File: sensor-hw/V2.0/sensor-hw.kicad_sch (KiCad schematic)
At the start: 0 parts

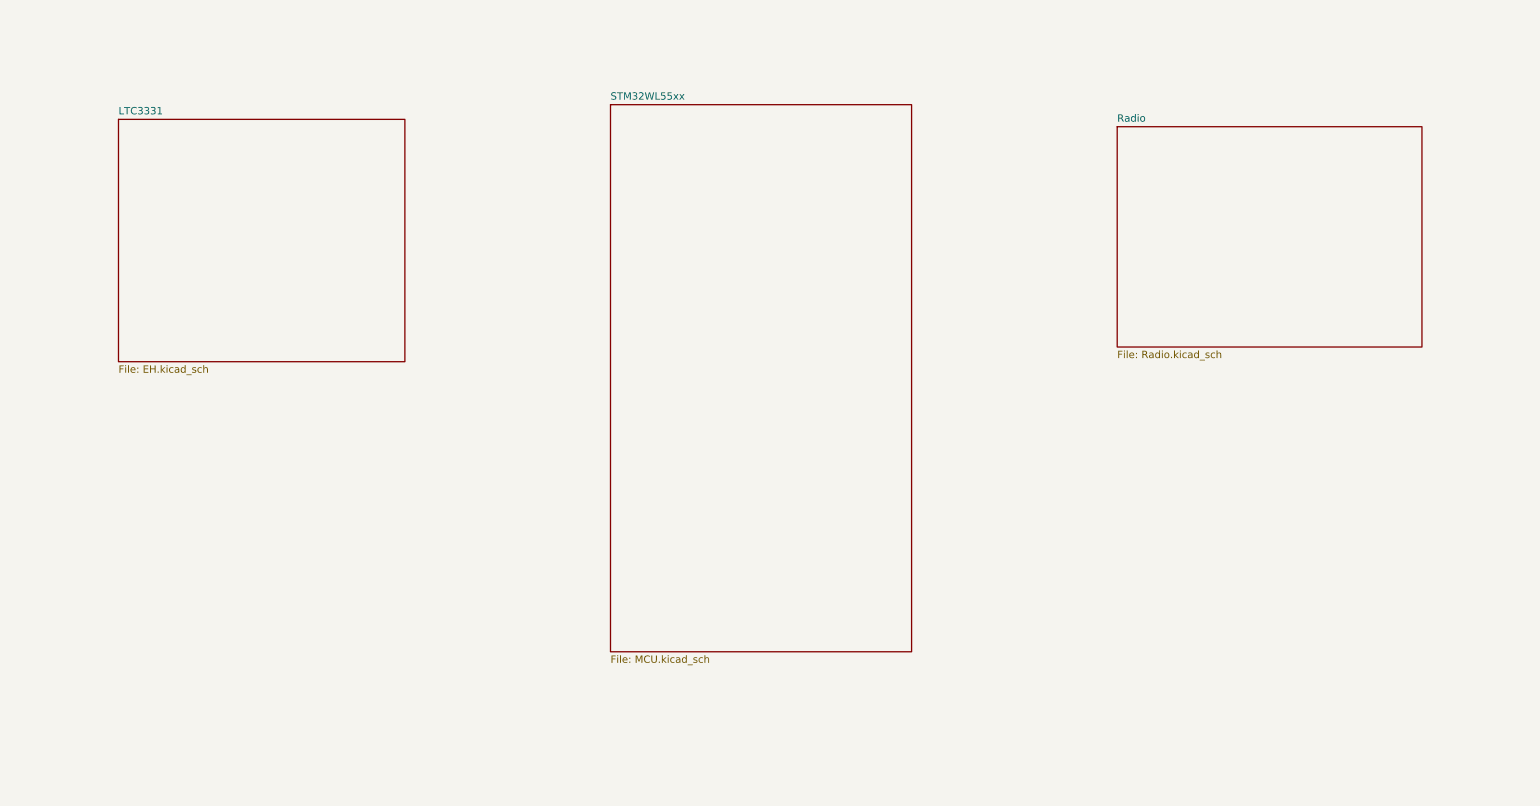
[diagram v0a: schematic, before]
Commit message: rearranged heirchal block wiring for better representation.
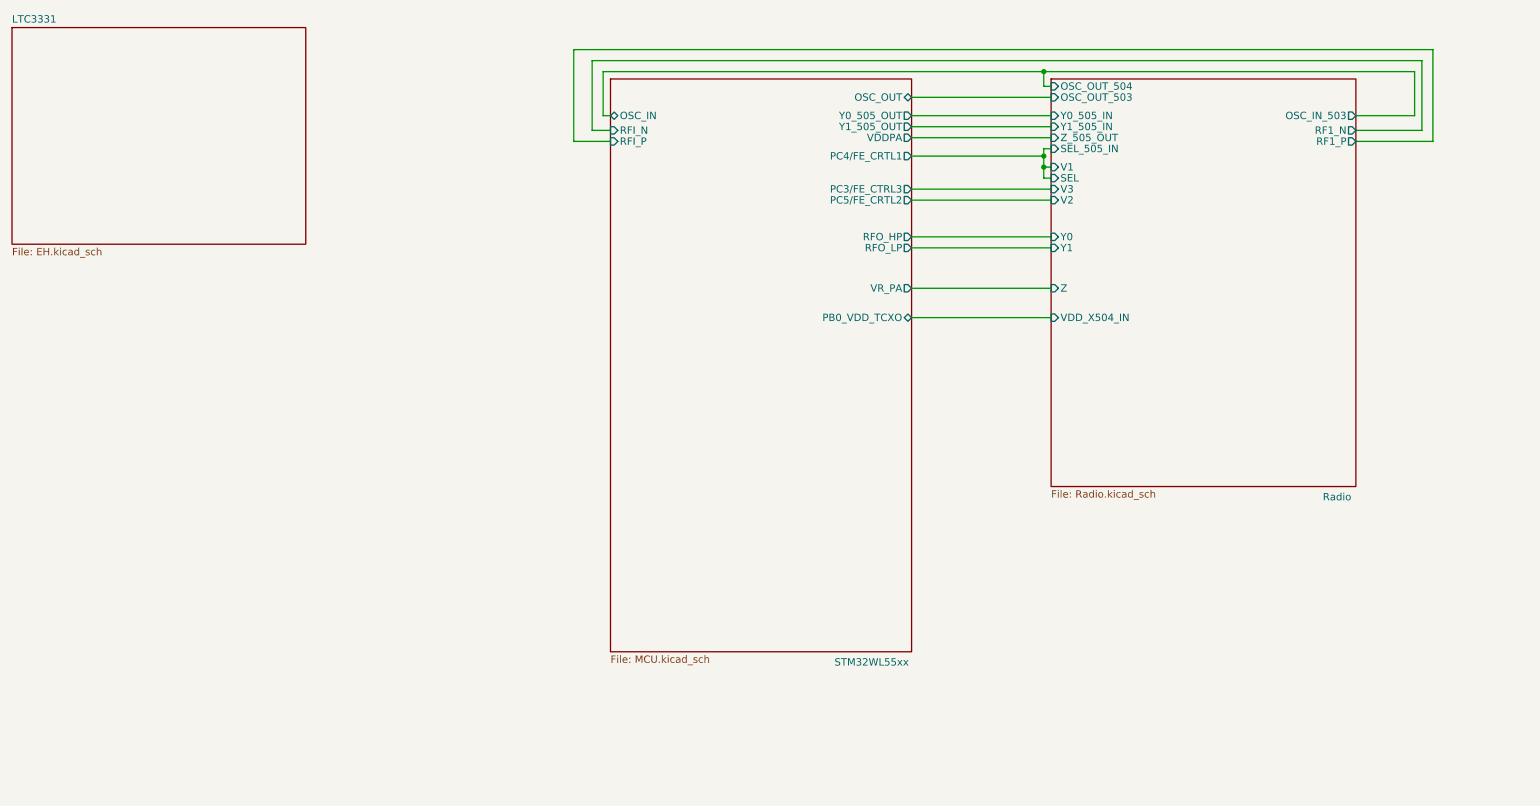
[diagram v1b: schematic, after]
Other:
- sheet Radio ports: added OSC_IN_503, OSC_OUT_503, OSC_OUT_504, RF1_N, RF1_P, SEL, SEL_505_IN, V1, V2, V3, VDD_X504_IN, Y0, Y0_505_IN, Y1, Y1_505_IN, Z, Z_505_OUT; removed none
- sheet STM32WL55xx ports: added OSC_IN, OSC_OUT, PB0_VDD_TCXO, PC3/FE_CTRL3, PC4/FE_CRTL1, PC5/FE_CRTL2, RFI_N, RFI_P, RFO_HP, RFO_LP, VDDPA, VR_PA, Y0_505_OUT, Y1_505_OUT; removed none
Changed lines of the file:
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@@
 (kicad_sch (version 20230121) (generator eeschema)
   (paper "A4")
-  (sheet (at 34.925 37.465) (size 49.53 41.91) (fields_autoplaced)
+  (junction (at 194.945 45.72) (diameter 0) (color 0 0 0 0)
+  )
+  (junction (at 194.945 29.21) (diameter 0) (color 0 0 0 0)
+  )
+  (junction (at 194.945 43.815) (diameter 0) (color 0 0 0 0)
+  )
+  (wire (pts (xy 260.35 39.37) (xy 260.35 27.305))
+    (stroke (width 0) (type default))
+  )
+  (wire (pts (xy 194.945 47.625) (xy 196.215 47.625))
+    (stroke (width 0) (type default))
+  )
+  (wire (pts (xy 172.085 33.655) (xy 196.215 33.655))
+    (stroke (width 0) (type default))
+  )
+  (wire (pts (xy 172.085 49.53) (xy 196.215 49.53))
+    (stroke (width 0) (type default))
+  )
+  (wire (pts (xy 172.085 57.785) (xy 196.215 57.785))
+    (stroke (width 0) (type default))
+  )
+  (wire (pts (xy 196.215 31.75) (xy 194.945 31.75))
+    (stroke (width 0) (type default))
+  )
+  (wire (pts (xy 194.945 45.72) (xy 196.215 45.72))
+    (stroke (width 0) (type default))
+  )
+  (wire (pts (xy 172.085 66.675) (xy 196.215 66.675))
+    (stroke (width 0) (type default))
+  )
+  (wire (pts (xy 172.085 36.83) (xy 196.215 36.83))
+    (stroke (width 0) (type default))
+  )
+  (wire (pts (xy 194.945 31.75) (xy 194.945 29.21))
+    (stroke (width 0) (type default))
+  )
+  (wire (pts (xy 172.085 38.735) (xy 196.215 38.735))
+    (stroke (width 0) (type default))
+  )
+  (wire (pts (xy 113.665 41.275) (xy 120.015 41.275))
+    (stroke (width 0) (type default))
+  )
+  (wire (pts (xy 194.945 43.815) (xy 194.945 45.72))
+    (stroke (width 0) (type default))
+  )
+  (wire (pts (xy 118.745 36.83) (xy 118.745 29.21))
+    (stroke (width 0) (type default))
+  )
+  (wire (pts (xy 172.085 51.435) (xy 196.215 51.435))
+    (stroke (width 0) (type default))
+  )
+  (wire (pts (xy 118.745 29.21) (xy 194.945 29.21))
+    (stroke (width 0) (type default))
+  )
+  (wire (pts (xy 262.255 41.275) (xy 262.255 25.4))
+    (stroke (width 0) (type default))
+  )
+  (wire (pts (xy 172.085 40.64) (xy 196.215 40.64))
+    (stroke (width 0) (type default))
+  )
+  (wire (pts (xy 172.085 59.69) (xy 196.215 59.69))
+    (stroke (width 0) (type default))
+  )
+  (wire (pts (xy 248.92 41.275) (xy 262.255 41.275))
+    (stroke (width 0) (type default))
+  )
+  (wire (pts (xy 172.085 43.815) (xy 194.945 43.815))
+    (stroke (width 0) (type default))
+  )
+  (wire (pts (xy 248.92 39.37) (xy 260.35 39.37))
+    (stroke (width 0) (type default))
+  )
+  (wire (pts (xy 116.84 27.305) (xy 116.84 39.37))
+    (stroke (width 0) (type default))
+  )
+  (wire (pts (xy 248.92 36.83) (xy 259.08 36.83))
+    (stroke (width 0) (type default))
+  )
+  (wire (pts (xy 194.945 29.21) (xy 259.08 29.21))
+    (stroke (width 0) (type default))
+  )
+  (wire (pts (xy 262.255 25.4) (xy 113.665 25.4))
+    (stroke (width 0) (type default))
+  )
+  (wire (pts (xy 172.085 71.755) (xy 196.215 71.755))
+    (stroke (width 0) (type default))
+  )
+  (wire (pts (xy 260.35 27.305) (xy 116.84 27.305))
+    (stroke (width 0) (type default))
+  )
+  (wire (pts (xy 113.665 25.4) (xy 113.665 41.275))
+    (stroke (width 0) (type default))
+  )
+  (wire (pts (xy 120.015 36.83) (xy 118.745 36.83))
+    (stroke (width 0) (type default))
+  )
+  (wire (pts (xy 194.945 43.815) (xy 194.945 42.545))
+    (stroke (width 0) (type default))
+  )
+  (wire (pts (xy 259.08 29.21) (xy 259.08 36.83))
+    (stroke (width 0) (type default))
+  )
+  (wire (pts (xy 194.945 45.72) (xy 194.945 47.625))
+    (stroke (width 0) (type default))
+  )
+  (wire (pts (xy 194.945 42.545) (xy 196.215 42.545))
+    (stroke (width 0) (type default))
+  )
+  (wire (pts (xy 116.84 39.37) (xy 120.015 39.37))
+    (stroke (width 0) (type default))
+  )
+  (sheet (at 16.51 21.59) (size 50.8 37.465) (fields_autoplaced)
     (stroke (width 0.1524) (type solid))
     (fill (color 0 0 0 0.0000))
-    (property "Sheetname" "LTC3331" (at 34.925 36.7534 0)
+    (property "Sheetname" "LTC3331" (at 16.51 20.8784 0)
       (effects (font (size 1.27 1.27)) (justify left bottom))
     )
-    (property "Sheetfile" "EH.kicad_sch" (at 34.925 79.9596 0)
+    (property "Sheetfile" "EH.kicad_sch" (at 16.51 59.6396 0)
       (effects (font (size 1.27 1.27)) (justify left top))
     )
@@
     )
   )
-  (sheet (at 120.015 34.925) (size 52.07 94.615) (fields_autoplaced)
+  (sheet (at 120.015 30.48) (size 52.07 99.06)
     (stroke (width 0.1524) (type solid))
     (fill (color 0 0 0 0.0000))
-    (property "Sheetname" "STM32WL55xx" (at 120.015 34.2134 0)
+    (property "Sheetname" "STM32WL55xx" (at 158.75 132.08 0)
       (effects (font (size 1.27 1.27)) (justify left bottom))
     )
     (property "Sheetfile" "MCU.kicad_sch" (at 120.015 130.1246 0)
       (effects (font (size 1.27 1.27)) (justify left top))
+    )
+    (pin "Y1_505_OUT" output (at 172.085 38.735 0)
+      (effects (font (size 1.27 1.27)) (justify right))
+    )
+    (pin "PC3{slash}FE_CTRL3" output (at 172.085 49.53 0)
+      (effects (font (size 1.27 1.27)) (justify right))
+    )
+    (pin "PC4{slash}FE_CRTL1" output (at 172.085 43.815 0)
+      (effects (font (size 1.27 1.27)) (justify right))
+    )
+    (pin "PC5{slash}FE_CRTL2" output (at 172.085 51.435 0)
+      (effects (font (size 1.27 1.27)) (justify right))
+    )
+    (pin "VDDPA" output (at 172.085 40.64 0)
+      (effects (font (size 1.27 1.27)) (justify right))
+    )
+    (pin "RFI_P" input (at 120.015 41.275 180)
+      (effects (font (size 1.27 1.27)) (justify left))
+    )
+    (pin "RFO_LP" output (at 172.085 59.69 0)
+      (effects (font (size 1.27 1.27)) (justify right))
+    )
+    (pin "OSC_OUT" bidirectional (at 172.085 33.655 0)
+      (effects (font (size 1.27 1.27)) (justify right))
+    )
+    (pin "OSC_IN" bidirectional (at 120.015 36.83 180)
+      (effects (font (size 1.27 1.27)) (justify left))
+    )
+    (pin "VR_PA" output (at 172.085 66.675 0)
+      (effects (font (size 1.27 1.27)) (justify right))
+    )
+    (pin "Y0_505_OUT" output (at 172.085 36.83 0)
+      (effects (font (size 1.27 1.27)) (justify right))
+    )
+    (pin "RFI_N" input (at 120.015 39.37 180)
+      (effects (font (size 1.27 1.27)) (justify left))
+    )
+    (pin "RFO_HP" output (at 172.085 57.785 0)
+      (effects (font (size 1.27 1.27)) (justify right))
+    )
+    (pin "PB0_VDD_TCXO" bidirectional (at 172.085 71.755 0)
+      (effects (font (size 1.27 1.27)) (justify right))
     )
     (instances
@@
     )
   )
-  (sheet (at 207.645 38.735) (size 52.705 38.1) (fields_autoplaced)
+  (sheet (at 196.215 30.48) (size 52.705 70.485)
     (stroke (width 0.1524) (type solid))
     (fill (color 0 0 0 0.0000))
-    (property "Sheetname" "Radio" (at 207.645 38.0234 0)
+    (property "Sheetname" "Radio" (at 243.205 103.505 0)
       (effects (font (size 1.27 1.27)) (justify left bottom))
     )
-    (property "Sheetfile" "Radio.kicad_sch" (at 207.645 77.4196 0)
+    (property "Sheetfile" "Radio.kicad_sch" (at 196.215 101.5496 0)
       (effects (font (size 1.27 1.27)) (justify left top))
     )
+    (pin "SEL_505_IN" input (at 196.215 42.545 180)
+      (effects (font (size 1.27 1.27)) (justify left))
+    )
+    (pin "V3" input (at 196.215 49.53 180)
+      (effects (font (size 1.27 1.27)) (justify left))
+    )
+    (pin "Y1" input (at 196.215 59.69 180)
+      (effects (font (size 1.27 1.27)) (justify left))
+    )
+    (pin "Z_505_OUT" input (at 196.215 40.64 180)
+      (effects (font (size 1.27 1.27)) (justify left))
+    )
+    (pin "Y0" input (at 196.215 57.785 180)
+      (effects (font (size 1.27 1.27)) (justify left))
+    )
+    (pin "RF1_N" output (at 248.92 39.37 0)
+      (effects (font (size 1.27 1.27)) (justify right))
+    )
+    (pin "V1" input (at 196.215 45.72 180)
+      (effects (font (size 1.27 1.27)) (justify left))
+    )
+    (pin "RF1_P" output (at 248.92 41.275 0)
+      (effects (font (size 1.27 1.27)) (justify right))
+    )
+    (pin "VDD_X504_IN" input (at 196.215 71.755 180)
+      (effects (font (size 1.27 1.27)) (justify left))
+    )
+    (pin "OSC_IN_503" output (at 248.92 36.83 0)
+      (effects (font (size 1.27 1.27)) (justify right))
+    )
+    (pin "OSC_OUT_504" input (at 196.215 31.75 180)
+      (effects (font (size 1.27 1.27)) (justify left))
+    )
+    (pin "OSC_OUT_503" input (at 196.215 33.655 180)
+      (effects (font (size 1.27 1.27)) (justify left))
+    )
+    (pin "Z" input (at 196.215 66.675 180)
+      (effects (font (size 1.27 1.27)) (justify left))
+    )
+    (pin "Y0_505_IN" input (at 196.215 36.83 180)
+      (effects (font (size 1.27 1.27)) (justify left))
+    )
+    (pin "Y1_505_IN" input (at 196.215 38.735 180)
+      (effects (font (size 1.27 1.27)) (justify left))
+    )
+    (pin "V2" input (at 196.215 51.435 180)
+      (effects (font (size 1.27 1.27)) (justify left))
+    )
+    (pin "SEL" input (at 196.215 47.625 180)
+      (effects (font (size 1.27 1.27)) (justify left))
+    )
     (instances

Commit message: Added the Power section.
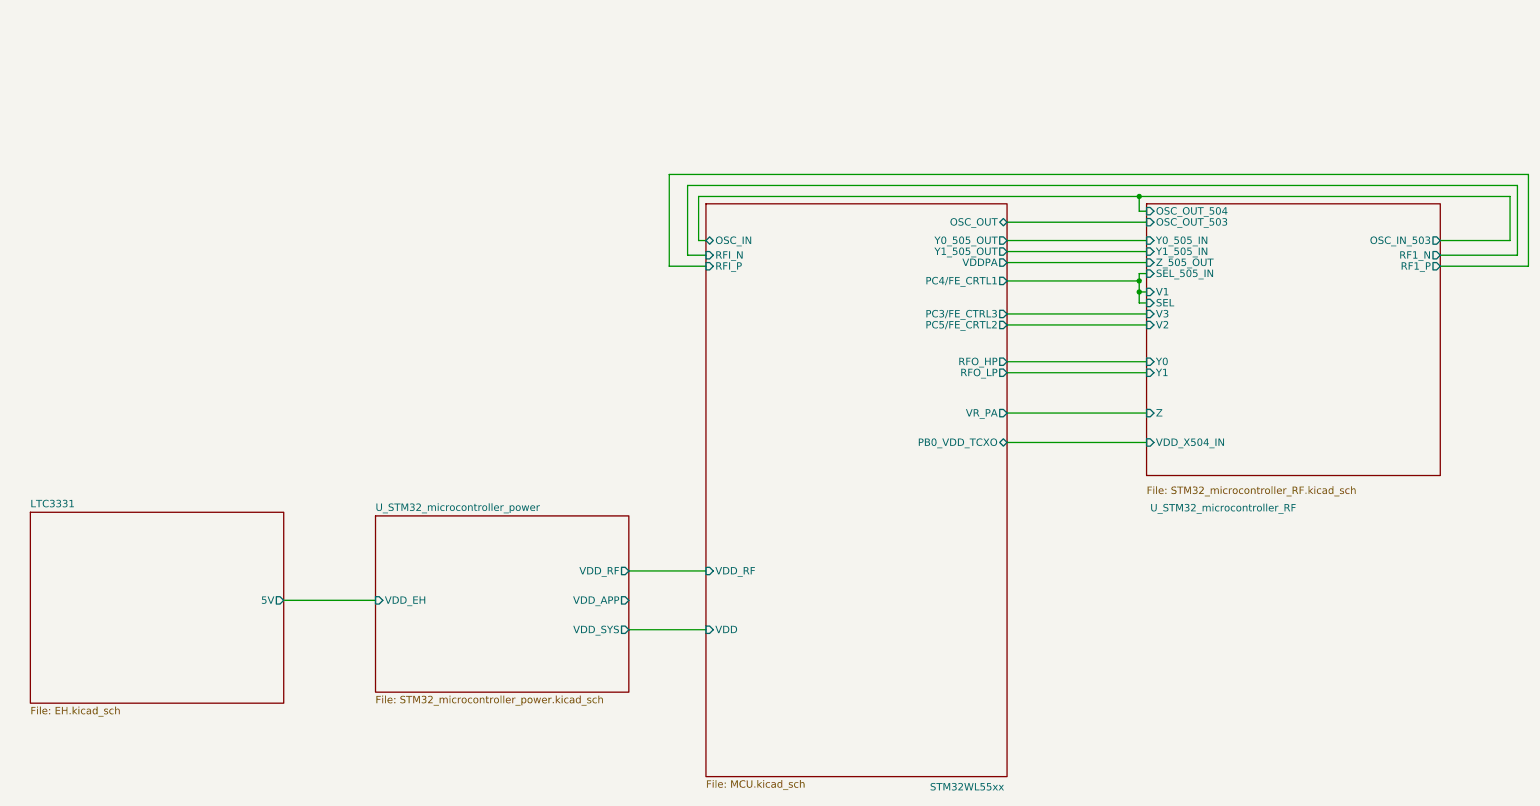
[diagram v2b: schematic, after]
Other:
- sheet Radio renamed U_STM32_microcontroller_RF
- added sheet U_STM32_microcontroller_power (STM32_microcontroller_power.kicad_sch)
- sheet LTC3331 ports: added 5V; removed none
- sheet STM32WL55xx ports: added VDD, VDD_RF; removed none
- sheet U_STM32_microcontroller_RF: file Radio.kicad_sch -> STM32_microcontroller_RF.kicad_sch
